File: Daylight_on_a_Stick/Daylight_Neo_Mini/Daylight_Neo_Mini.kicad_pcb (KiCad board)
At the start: 2 copper layers, 170 x 11 mm, 22 parts, among them J1 IN, J2 OUT

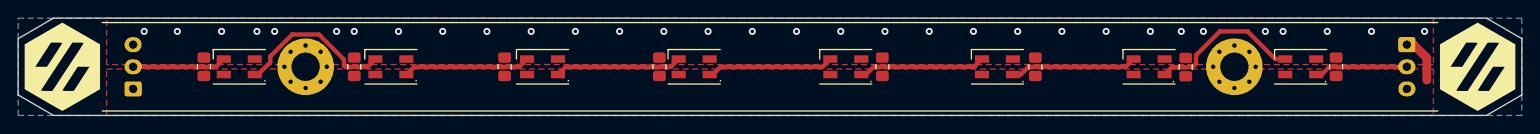
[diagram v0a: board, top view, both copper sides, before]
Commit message: Fixed some Layout LED footprint issues
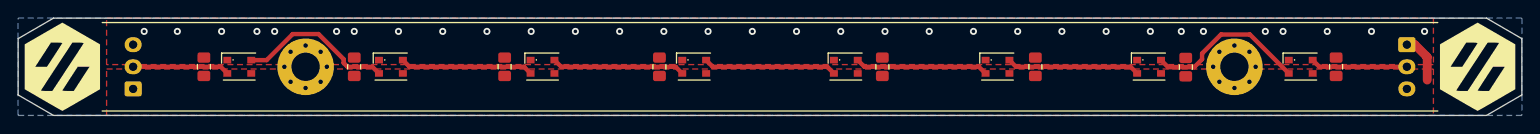
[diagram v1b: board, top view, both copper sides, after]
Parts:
- D1, D2, D3, D4, D5, D6, D7, D8: footprint LED_SMD:LED_SK6812MINI_PLCC4_3.5x3.5mm_P1.75mm -> Daylight:XL-3528RGBW-WS2812B
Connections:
- D1 pad 1: Net-(D1-Pad1) -> GND
- D1 pad 2: GND -> Dstart
- D1 pad 3: Dstart -> +5V
- D1 pad 4: +5V -> Net-(D1-Pad4)
- D2 pad 1: Net-(D2-Pad1) -> GND
- D2 pad 2: GND -> Net-(D1-Pad4)
- D2 pad 3: Net-(D1-Pad1) -> +5V
- D2 pad 4: +5V -> Net-(D2-Pad4)
- D3 pad 1: Net-(D3-Pad1) -> GND
- D3 pad 2: GND -> Net-(D2-Pad4)
- D3 pad 3: Net-(D2-Pad1) -> +5V
- D3 pad 4: +5V -> Net-(D3-Pad4)
- D4 pad 1: Net-(D4-Pad1) -> GND
- D4 pad 2: GND -> Net-(D3-Pad4)
- D4 pad 3: Net-(D3-Pad1) -> +5V
- D4 pad 4: +5V -> Net-(D4-Pad4)
- D5 pad 1: Net-(D5-Pad1) -> GND
- D5 pad 2: GND -> Net-(D4-Pad4)
- D5 pad 3: Net-(D4-Pad1) -> +5V
- D5 pad 4: +5V -> Net-(D5-Pad4)
- D6 pad 1: Net-(D6-Pad1) -> GND
- D6 pad 2: GND -> Net-(D5-Pad4)
- D6 pad 3: Net-(D5-Pad1) -> +5V
- D6 pad 4: +5V -> Net-(D6-Pad4)
- D7 pad 1: Net-(D7-Pad1) -> GND
- D7 pad 2: GND -> Net-(D6-Pad4)
- D7 pad 3: Net-(D6-Pad1) -> +5V
- D7 pad 4: +5V -> Net-(D7-Pad4)
- D8 pad 1: Dend -> GND
- D8 pad 2: GND -> Net-(D7-Pad4)
- D8 pad 3: Net-(D7-Pad1) -> +5V
- D8 pad 4: +5V -> Dend
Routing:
- net Net-(D7-Pad4): track 0.00 -> 18.5 mm
- net Net-(D1-Pad1): track 18.2 -> 0.00 mm
- net Net-(D1-Pad4): track 0.00 -> 17.8 mm
- net Net-(D7-Pad1): track 17.5 -> 0.00 mm
- net Net-(D4-Pad4): track 0.00 -> 15.1 mm
- net Net-(D3-Pad4): track 0.00 -> 15.1 mm
- net Net-(D2-Pad4): track 0.00 -> 15.1 mm
- net Net-(D6-Pad4): track 0.00 -> 15.1 mm
- net Net-(D5-Pad4): track 0.00 -> 15.1 mm
- net Net-(D5-Pad1): track 14.4 -> 0.00 mm
- net Net-(D3-Pad1): track 14.4 -> 0.00 mm
- net Net-(D6-Pad1): track 14.4 -> 0.00 mm
- net Net-(D2-Pad1): track 14.4 -> 0.00 mm
- net Net-(D4-Pad1): track 14.4 -> 0.00 mm
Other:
- board text added: "Daylight on a stick by Blamm Daybreak Neo Mini by Vector 3D V2.1"
- board text removed: "Daylight on a stick by Blamm Daybreak Neo Mini by Vector 3D V2"

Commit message: Daylight (all) V2.2
The JST XH silkscreen did not match the connectors very well so it has been adjusted.
Added small front silkscreen to indicate pins
Adjusted one connector on day_mini that was misplaced 1mm.
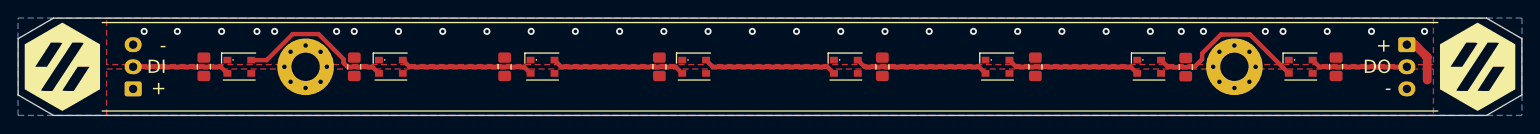
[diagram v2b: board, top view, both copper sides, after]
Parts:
- J1, J2: footprint Connector_JST:JST_XH_S3B-XH-A_1x03_P2.50mm_Horizontal -> Daylight:JST_XH_S3B-XH-A_1x03_P2.50mm_Horizontal Daylight
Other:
- board text added: "+ DO -"
- board text added: "- DI +"
- board text added: "Daylight on a stick by Blamm Daybreak Neo Mini by Vector 3D V2.2"
- board text removed: "Daylight on a stick by Blamm Daybreak Neo Mini by Vector 3D V2.1"

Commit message: Minor Updates
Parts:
- added G***: LOGO, LOGO, B.Cu at (133.3, 33.0)
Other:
- board text added: "Daylight on a stick by Blamm Daybreak Neo Mini by Vector 3D V2.3"
- board text removed: "Daylight on a stick by Blamm Daybreak Neo Mini by Vector 3D V2.2"

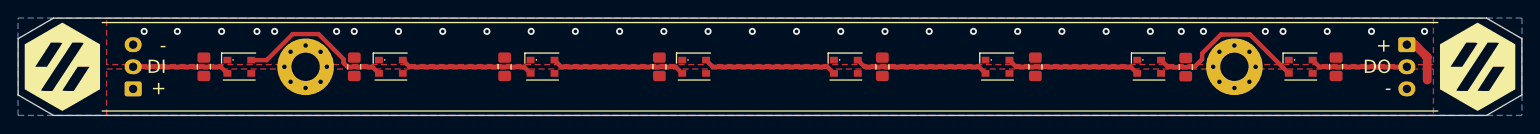
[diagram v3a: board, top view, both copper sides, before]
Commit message: Minor LED Updates
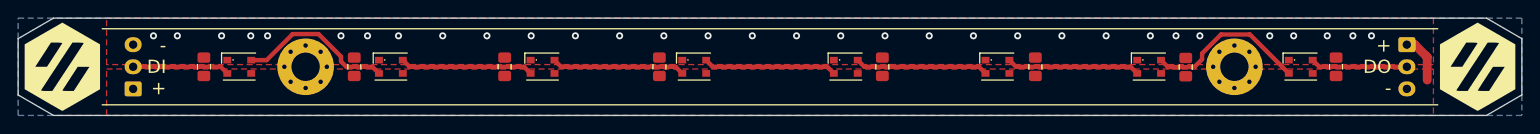
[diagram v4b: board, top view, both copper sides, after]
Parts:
- added REF**: Tab, kikit:Tab, F.Cu at (98.0, 27.5)
- added REF**: Tab, kikit:Tab, F.Cu at (98.0, 38.5)
- added REF**: Tab, kikit:Tab, F.Cu at (150.5, 27.5)
- added REF**: Tab, kikit:Tab, F.Cu at (45.5, 27.5)
- added REF**: Tab, kikit:Tab, F.Cu at (150.5, 38.5)
- added REF**: Tab, kikit:Tab, F.Cu at (45.5, 38.5)
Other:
- board text added: "Daylight on a stick by Blamm Daybreak Neo Mini by Vector 3D V2.4"
- board text removed: "Daylight on a stick by Blamm Daybreak Neo Mini by Vector 3D V2.3"
